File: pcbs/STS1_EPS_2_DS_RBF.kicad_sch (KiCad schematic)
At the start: 20 parts, among them Q1 2N7002, Q10 2N7002, Q13 2N7002, Q14 2N7002, Q15 2N7002, Q16 BSS83P, Q17 2N7002, Q6 2N7002, Q7 2N7002, Q8 BSS83P, Q9 2N7002

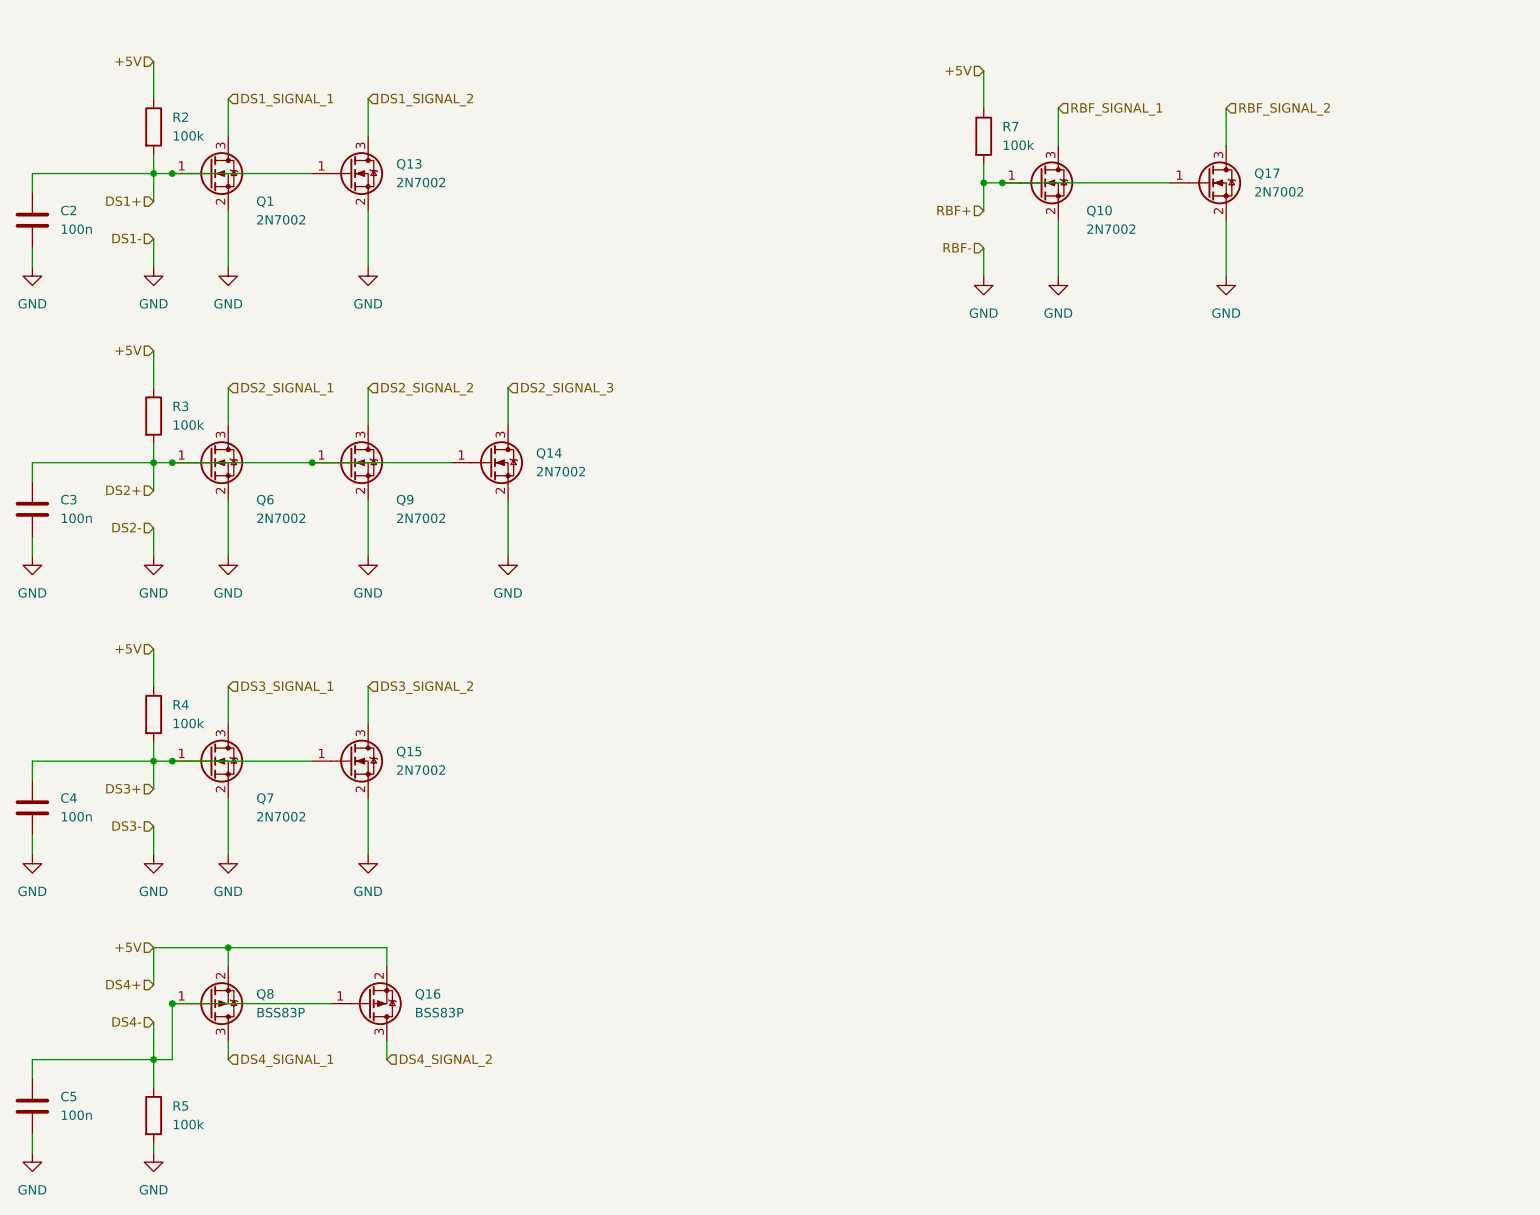
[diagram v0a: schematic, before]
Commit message: Added test points to STS1_EPS_2.
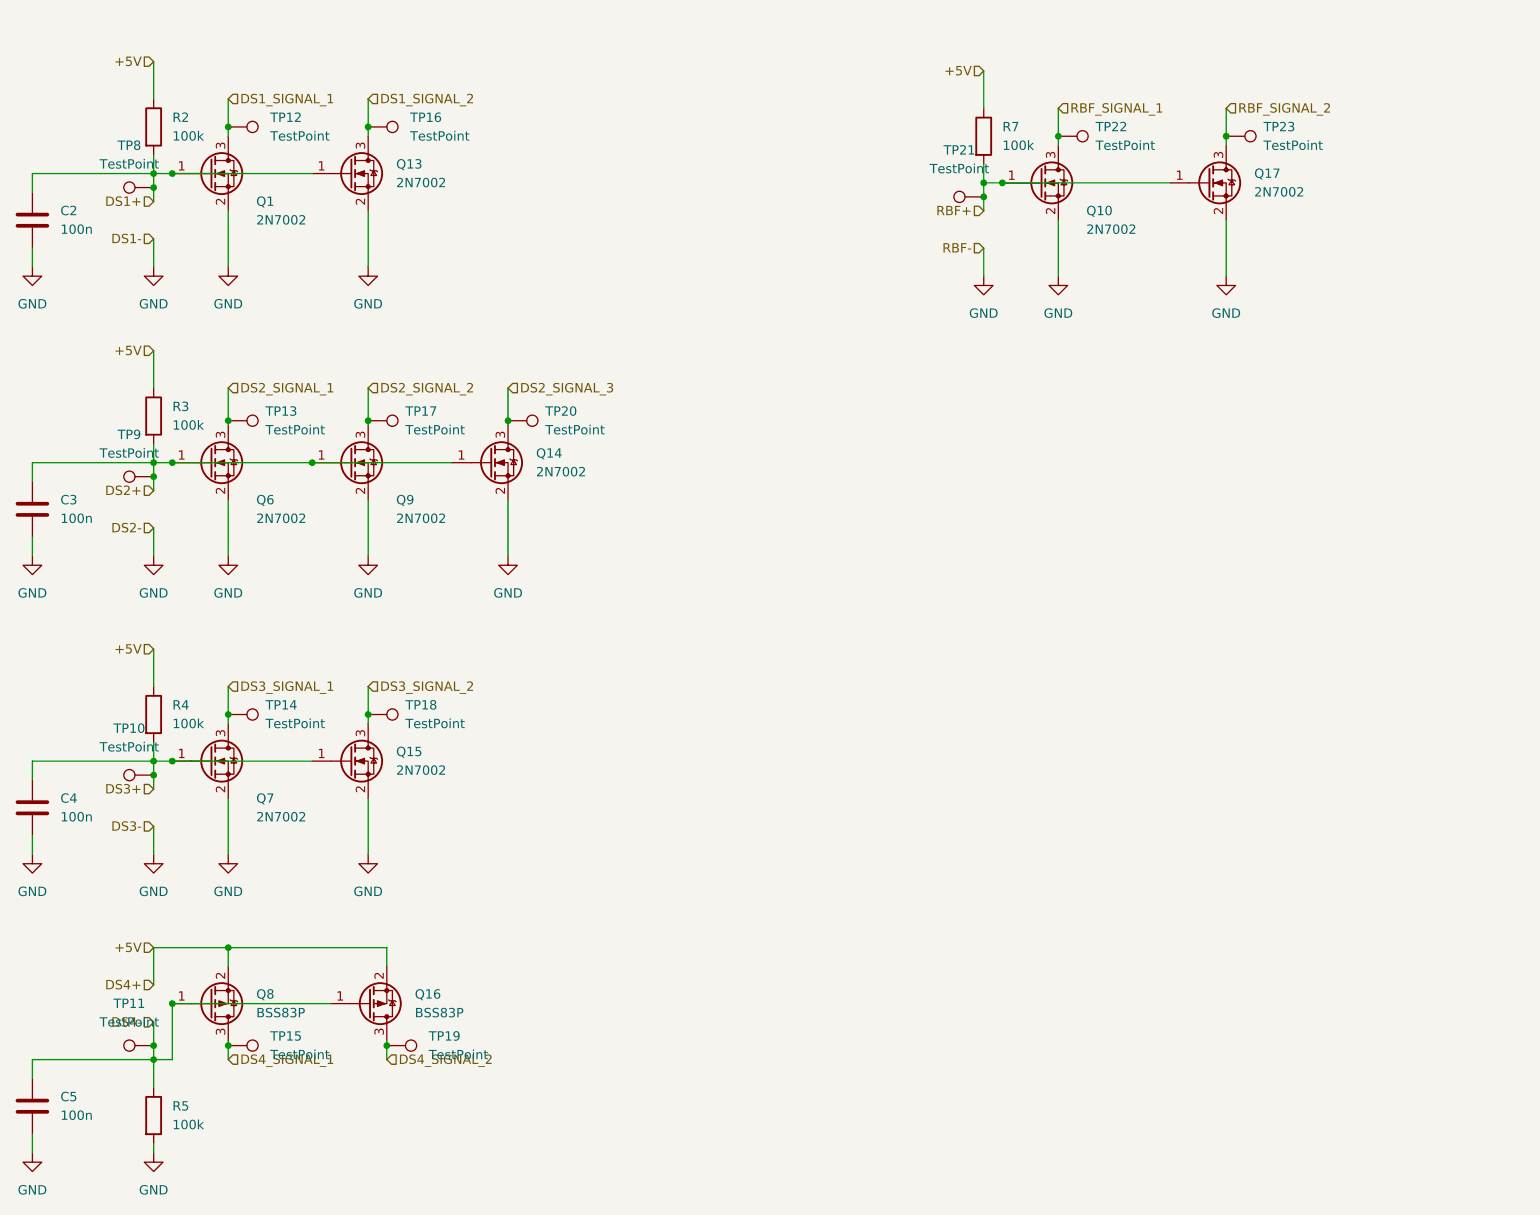
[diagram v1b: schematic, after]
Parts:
- added TP10, TP11, TP12, TP13, TP14, TP15, TP16, TP17, TP18, TP19, TP20, TP21, TP22, TP23, TP8, TP9: TestPoint, TestPoint:TestPoint_THTPad_D1.0mm_Drill0.5mm, symbol Connector:TestPoint
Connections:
- net DS1+: now also TP8.1
- net DS1_SIGNAL_1: now also TP12.1
- net DS1_SIGNAL_2: now also TP16.1
- net DS2+: now also TP9.1
- net DS2_SIGNAL_1: now also TP13.1
- net DS2_SIGNAL_2: now also TP17.1
- net DS2_SIGNAL_3: now also TP20.1
- net DS3+: now also TP10.1
- net DS3_SIGNAL_1: now also TP14.1
- net DS3_SIGNAL_2: now also TP18.1
- net DS4-: now also TP11.1
- net DS4_SIGNAL_1: now also TP15.1
- net DS4_SIGNAL_2: now also TP19.1
- net RBF+: now also TP21.1
- net RBF_SIGNAL_1: now also TP22.1
- net RBF_SIGNAL_2: now also TP23.1

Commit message: Worked on STS1_EPS_2.
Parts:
- renumbered C2 to C3, C3 to C4, C4 to C5, C5 to C6, Q1 to Q10, Q6 to Q11, Q7 to Q12, Q8 to Q13, Q13 to Q14, Q9 to Q15, Q15 to Q16, Q16 to Q17, Q14 to Q18, Q10 to Q19, Q17 to Q20, R2 to R25, R3 to R26, R4 to R27, R5 to R28, R7 to R29

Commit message: Worked on STS1_EPS_2.
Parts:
- removed C5, C6: 100n, Capacitor_SMD:C_0805_2012Metric, symbol Device:C
- removed Q12, Q16: 2N7002, Package_TO_SOT_SMD:SOT-23, symbol Transistor_FET:2N7002
- removed Q13, Q17: BSS83P, Package_TO_SOT_SMD:SOT-23, symbol Transistor_FET:BSS83P
- removed R27, R28: 100k, Resistor_SMD:R_0805_2012Metric, symbol Device:R
- removed TP14, TP15, TP18, TP19: TestPoint, TestPoint:TestPoint_THTPad_D1.0mm_Drill0.5mm, symbol Connector:TestPoint
- added Q1, Q7: 2N7002, Package_TO_SOT_SMD:SOT-23, symbol Transistor_FET:2N7002
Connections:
- net DS1+: now also Q7.1 (G)
- net GND: now also Q1.2 (S), Q7.2 (S)
- net RBF+: now also Q1.1 (G)
- net DS3+ renamed RBF_SIGNAL_3
- net RBF_SIGNAL_3: now also Q1.3 (D)
- net DS4- renamed DS1_SIGNAL_3
- net DS1_SIGNAL_3: now also Q7.3 (D)

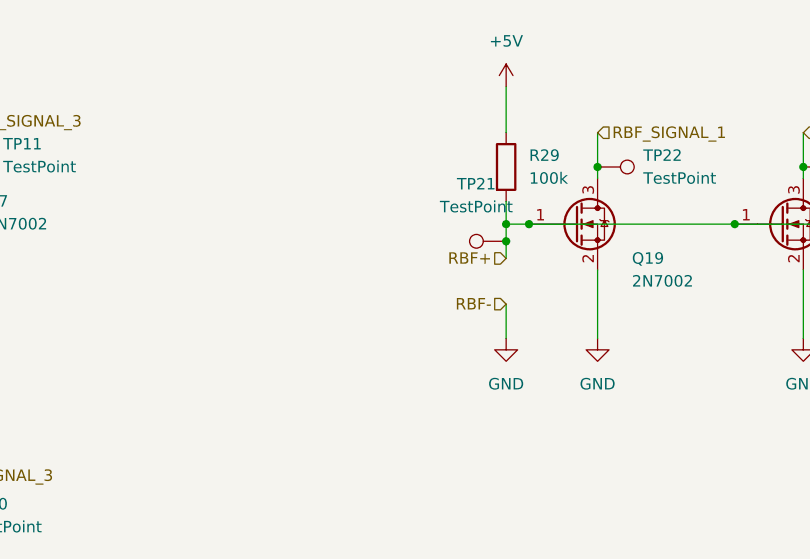
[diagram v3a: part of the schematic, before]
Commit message: STS1_EPS_2 no errors.
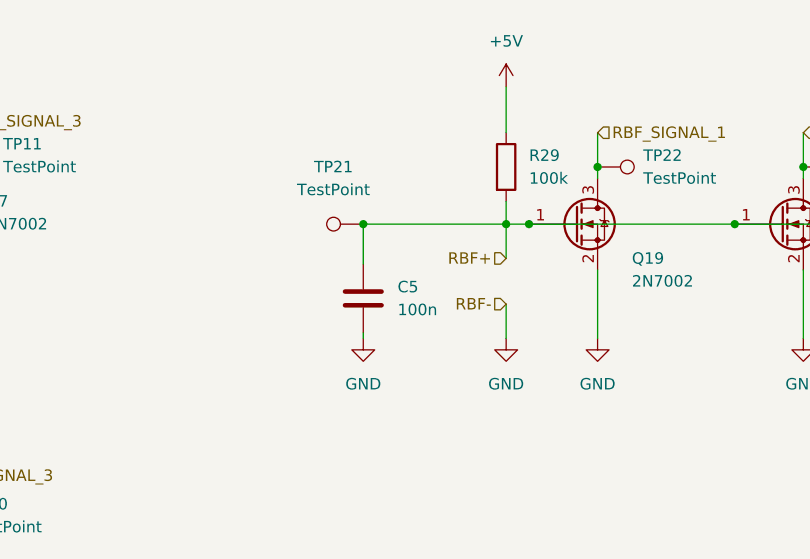
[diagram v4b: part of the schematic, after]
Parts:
- added C5: 100n, Capacitor_SMD:C_0805_2012Metric, symbol Device:C
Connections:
- net GND: now also C5.2
- net RBF+: now also C5.1
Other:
- moved on the sheet: TP21
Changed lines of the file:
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@@
   (junction (at 86.995 33.02) (diameter 0) (color 0 0 0 0)
   )
-  (junction (at 148.59 42.545) (diameter 0) (color 0 0 0 0)
+  (junction (at 132.715 40.64) (diameter 0) (color 0 0 0 0)
   )
   (junction (at 35.56 80.645) (diameter 0) (color 0 0 0 0)
@@
     (stroke (width 0) (type default) (color 0 0 0 0))
   )
+  (wire (pts (xy 148.59 38.1) (xy 148.59 40.64))
+    (stroke (width 0) (type default) (color 0 0 0 0))
+  )
   (wire (pts (xy 45.72 44.45) (xy 45.72 52.07))
     (stroke (width 0) (type default) (color 0 0 0 0))
@@
     (stroke (width 0) (type default) (color 0 0 0 0))
   )
-  (wire (pts (xy 148.59 42.545) (xy 148.59 44.45))
+  (wire (pts (xy 148.59 40.64) (xy 148.59 44.45))
     (stroke (width 0) (type default) (color 0 0 0 0))
   )
@@
     (stroke (width 0) (type default) (color 0 0 0 0))
   )
+  (wire (pts (xy 132.715 40.64) (xy 148.59 40.64))
+    (stroke (width 0) (type default) (color 0 0 0 0))
+  )
   (wire (pts (xy 38.1 78.74) (xy 57.15 78.74))
     (stroke (width 0) (type default) (color 0 0 0 0))
@@
     (stroke (width 0) (type default) (color 0 0 0 0))
   )
+  (wire (pts (xy 132.715 52.705) (xy 132.715 53.34))
+    (stroke (width 0) (type default) (color 0 0 0 0))
+  )
   (wire (pts (xy 205.105 45.72) (xy 205.105 53.34))
     (stroke (width 0) (type default) (color 0 0 0 0))
@@
     (stroke (width 0) (type default) (color 0 0 0 0))
   )
-  (wire (pts (xy 148.59 38.1) (xy 148.59 40.64))
-    (stroke (width 0) (type default) (color 0 0 0 0))
-  )
   (wire (pts (xy 45.72 68.58) (xy 45.72 73.025))
     (stroke (width 0) (type default) (color 0 0 0 0))
@@
     (stroke (width 0) (type default) (color 0 0 0 0))
   )
-  (wire (pts (xy 148.59 40.64) (xy 148.59 42.545))
+  (wire (pts (xy 132.715 40.64) (xy 132.715 45.085))
     (stroke (width 0) (type default) (color 0 0 0 0))
   )
@@
     )
     (property "Datasheet" "" (id 3) (at 148.59 53.34 0)
+      (effects (font (size 1.27 1.27)) hide)
+    )
+    (pin "1")
+  )
+  (symbol (lib_id "power:GND") (at 132.715 53.34 0) (unit 1)
+    (in_bom yes) (on_board yes) (fields_autoplaced)
+    (property "Reference" "#PWR0124" (id 0) (at 132.715 59.69 0)
+      (effects (font (size 1.27 1.27)) hide)
+    )
+    (property "Value" "GND" (id 1) (at 132.715 58.42 0))
+    (property "Footprint" "" (id 2) (at 132.715 53.34 0)
+      (effects (font (size 1.27 1.27)) hide)
+    )
+    (property "Datasheet" "" (id 3) (at 132.715 53.34 0)
       (effects (font (size 1.27 1.27)) hide)
     )
@@
     (pin "1")
   )
-  (symbol (lib_id "Connector:TestPoint") (at 148.59 42.545 90) (unit 1)
-    (in_bom yes) (on_board yes) (fields_autoplaced)
-    (property "Reference" "TP21" (id 0) (at 145.288 36.195 90))
-    (property "Value" "TestPoint" (id 1) (at 145.288 38.735 90))
-    (property "Footprint" "TestPoint:TestPoint_THTPad_D1.0mm_Drill0.5mm" (id 2) (at 148.59 37.465 0)
-      (effects (font (size 1.27 1.27)) hide)
-    )
-    (property "Datasheet" "~" (id 3) (at 148.59 37.465 0)
+  (symbol (lib_id "Connector:TestPoint") (at 132.715 40.64 90) (unit 1)
+    (in_bom yes) (on_board yes) (fields_autoplaced)
+    (property "Reference" "TP21" (id 0) (at 129.413 34.29 90))
+    (property "Value" "TestPoint" (id 1) (at 129.413 36.83 90))
+    (property "Footprint" "TestPoint:TestPoint_THTPad_D1.0mm_Drill0.5mm" (id 2) (at 132.715 35.56 0)
+      (effects (font (size 1.27 1.27)) hide)
+    )
+    (property "Datasheet" "~" (id 3) (at 132.715 35.56 0)
       (effects (font (size 1.27 1.27)) hide)
     )
@@
     (pin "1")
   )
+  (symbol (lib_id "Device:C") (at 132.715 48.895 0) (unit 1)
+    (in_bom yes) (on_board yes) (fields_autoplaced)
+    (property "Reference" "C5" (id 0) (at 136.525 47.6249 0)
+      (effects (font (size 1.27 1.27)) (justify left))
+    )
+    (property "Value" "100n" (id 1) (at 136.525 50.1649 0)
+      (effects (font (size 1.27 1.27)) (justify left))
+    )
+    (property "Footprint" "Capacitor_SMD:C_0805_2012Metric" (id 2) (at 133.6802 52.705 0)
+      (effects (font (size 1.27 1.27)) hide)
+    )
+    (property "Datasheet" "~" (id 3) (at 132.715 48.895 0)
+      (effects (font (size 1.27 1.27)) hide)
+    )
+    (pin "1")
+    (pin "2")
+  )
   (symbol (lib_id "power:GND") (at 45.72 52.07 0) (unit 1)

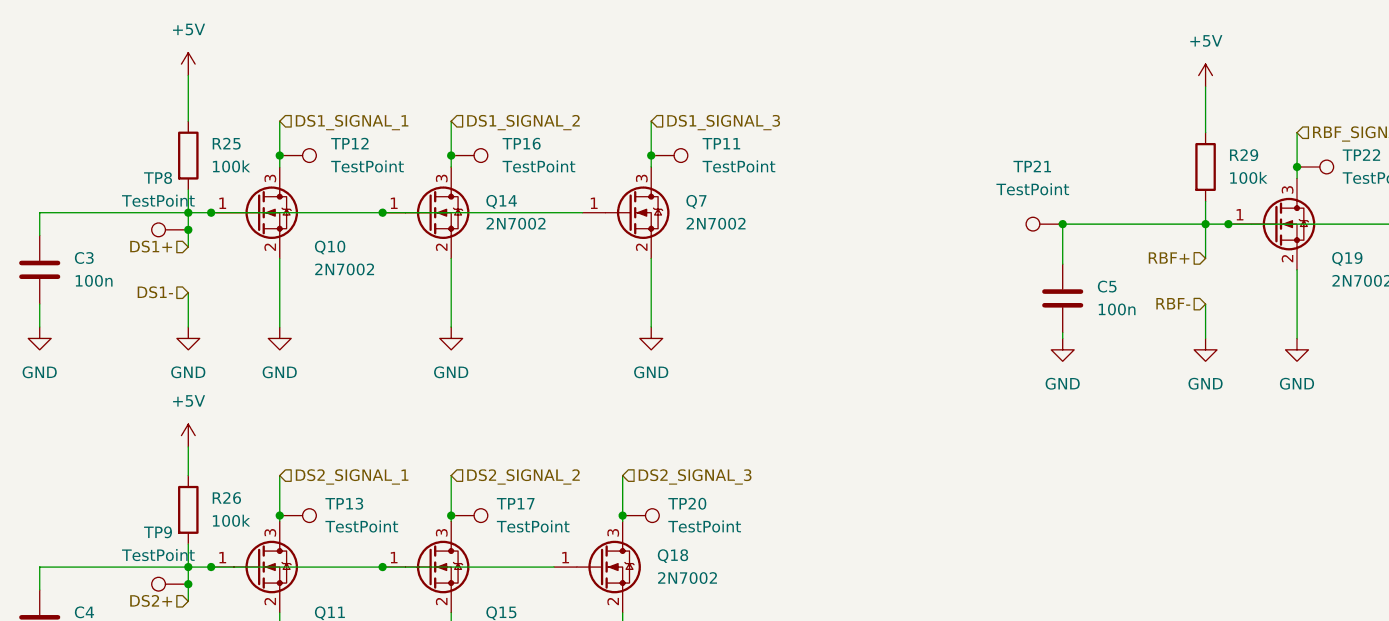
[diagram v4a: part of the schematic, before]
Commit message: Added a logic voltage, so that the deployment circuit breaker FETs also work, when battery is fails.
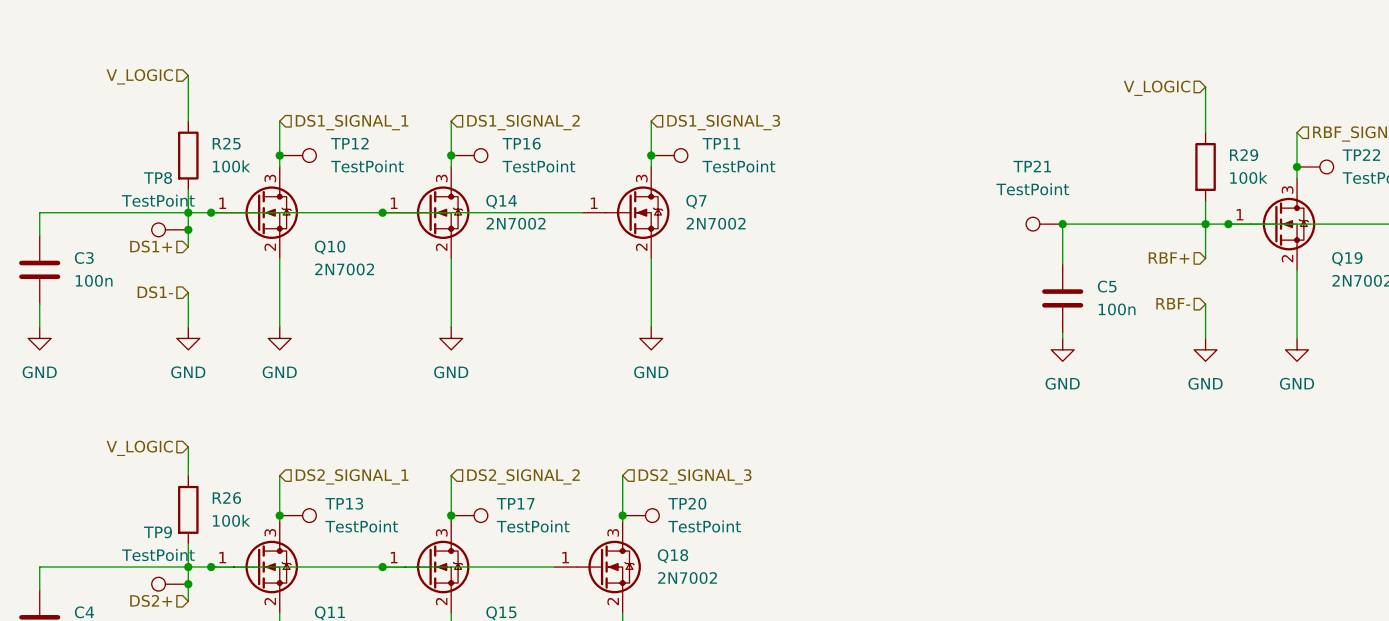
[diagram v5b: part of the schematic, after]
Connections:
- net +5V renamed V_LOGIC
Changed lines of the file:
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@@
     (effects (font (size 1.27 1.27)) (justify left))
+  )
+  (hierarchical_label "V_LOGIC" (shape input) (at 148.59 25.4 180)
+    (effects (font (size 1.27 1.27)) (justify right))
   )
   (hierarchical_label "DS2_SIGNAL_3" (shape input) (at 83.82 68.58 0)
@@
     (effects (font (size 1.27 1.27)) (justify right))
   )
+  (hierarchical_label "V_LOGIC" (shape input) (at 35.56 24.13 180)
+    (effects (font (size 1.27 1.27)) (justify right))
+  )
   (hierarchical_label "DS2-" (shape input) (at 35.56 87.63 180)
     (effects (font (size 1.27 1.27)) (justify right))
@@
   )
   (hierarchical_label "DS2+" (shape input) (at 35.56 82.55 180)
+    (effects (font (size 1.27 1.27)) (justify right))
+  )
+  (hierarchical_label "V_LOGIC" (shape input) (at 35.56 65.405 180)
     (effects (font (size 1.27 1.27)) (justify right))
   )
@@
     (pin "3")
   )
-  (symbol (lib_id "power:+5V") (at 35.56 24.13 0) (unit 1)
-    (in_bom yes) (on_board yes) (fields_autoplaced)
-    (property "Reference" "#PWR0116" (id 0) (at 35.56 27.94 0)
-      (effects (font (size 1.27 1.27)) hide)
-    )
-    (property "Value" "+5V" (id 1) (at 35.56 19.05 0))
-    (property "Footprint" "" (id 2) (at 35.56 24.13 0)
-      (effects (font (size 1.27 1.27)) hide)
-    )
-    (property "Datasheet" "" (id 3) (at 35.56 24.13 0)
-      (effects (font (size 1.27 1.27)) hide)
-    )
-    (pin "1")
-  )
   (symbol (lib_id "power:GND") (at 181.61 53.34 0) (unit 1)
     (in_bom yes) (on_board yes) (fields_autoplaced)
@@
     (pin "3")
   )
-  (symbol (lib_id "power:+5V") (at 148.59 25.4 0) (unit 1)
-    (in_bom yes) (on_board yes) (fields_autoplaced)
-    (property "Reference" "#PWR0118" (id 0) (at 148.59 29.21 0)
-      (effects (font (size 1.27 1.27)) hide)
-    )
-    (property "Value" "+5V" (id 1) (at 148.59 20.32 0))
-    (property "Footprint" "" (id 2) (at 148.59 25.4 0)
-      (effects (font (size 1.27 1.27)) hide)
-    )
-    (property "Datasheet" "" (id 3) (at 148.59 25.4 0)
-      (effects (font (size 1.27 1.27)) hide)
-    )
-    (pin "1")
-  )
   (symbol (lib_id "power:GND") (at 158.75 53.34 0) (unit 1)
     (in_bom yes) (on_board yes) (fields_autoplaced)
@@
       (effects (font (size 1.27 1.27)) hide)
     )
-    (pin "1")
-  )
-  (symbol (lib_id "power:+5V") (at 35.56 65.405 0) (unit 1)
-    (in_bom yes) (on_board yes) (fields_autoplaced)
-    (property "Reference" "#PWR0117" (id 0) (at 35.56 69.215 0)
-      (effects (font (size 1.27 1.27)) hide)
-    )
-    (property "Value" "+5V" (id 1) (at 35.56 60.325 0))
-    (property "Footprint" "" (id 2) (at 35.56 65.405 0)
-      (effects (font (size 1.27 1.27)) hide)
-    )
-    (property "Datasheet" "" (id 3) (at 35.56 65.405 0)
-      (effects (font (size 1.27 1.27)) hide)
-    )
